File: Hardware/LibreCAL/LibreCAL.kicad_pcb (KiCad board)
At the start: 4 copper layers, 55 x 73.5 mm, 132 parts, among them J1 901-10510-2, J2 901-10510-2, J3 901-10510-2, J4 901-10510-2, J5 USB_C_Receptacle_USB2.0, J6 TC2030-ARM, Q1 IRLML2060, SW1 TL3301NF160QG, SW2 TL3301CF160QG, SW3 TL3301CF160QG, U1 PE426462, U2 PE426462, U3 PE426462, U4 PE426462, U5 W25Q16JVSNIQ, U6 IP4234CZ6, U7 RP2040, U8 W25Q16JVSNIQ, U9 MIC5528-3.3YMT-TR, Y1 ECS-120-8-36-CKM-TR3

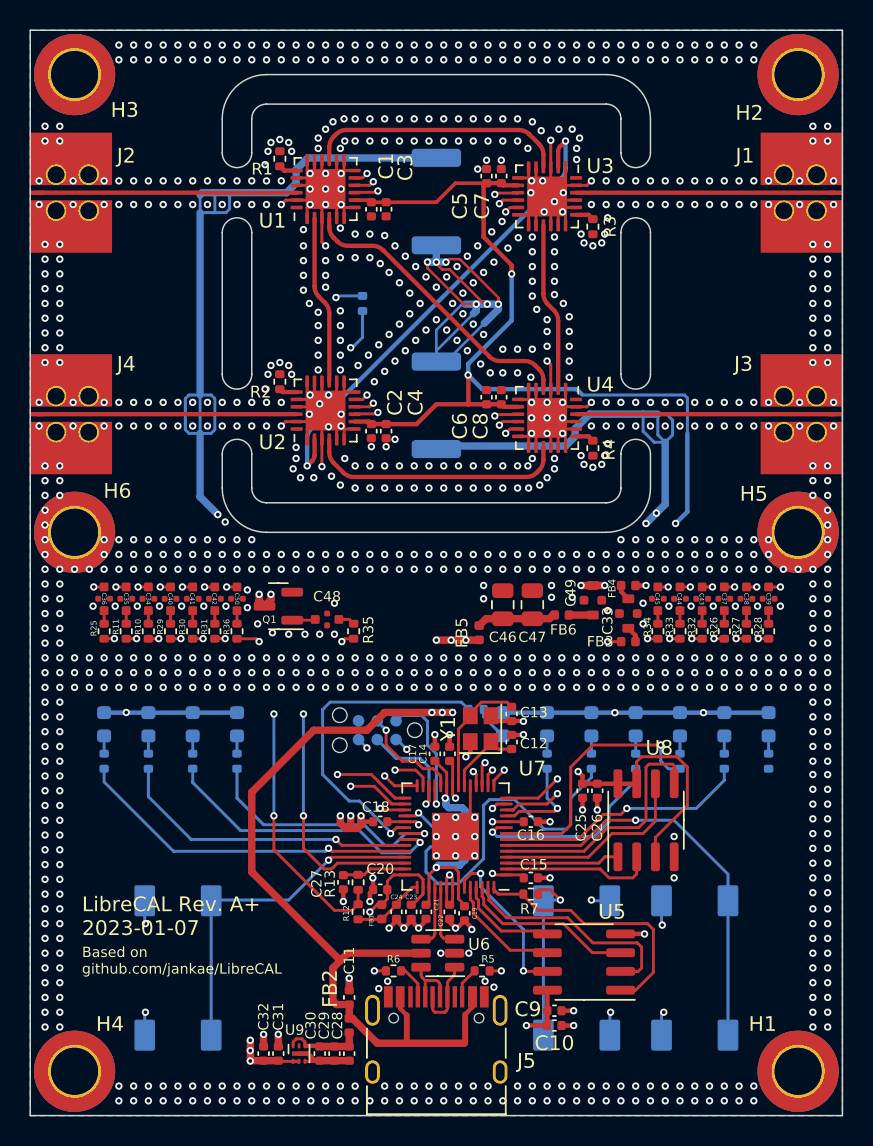
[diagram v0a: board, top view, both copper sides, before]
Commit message: update to larger flash for calibration coefficients
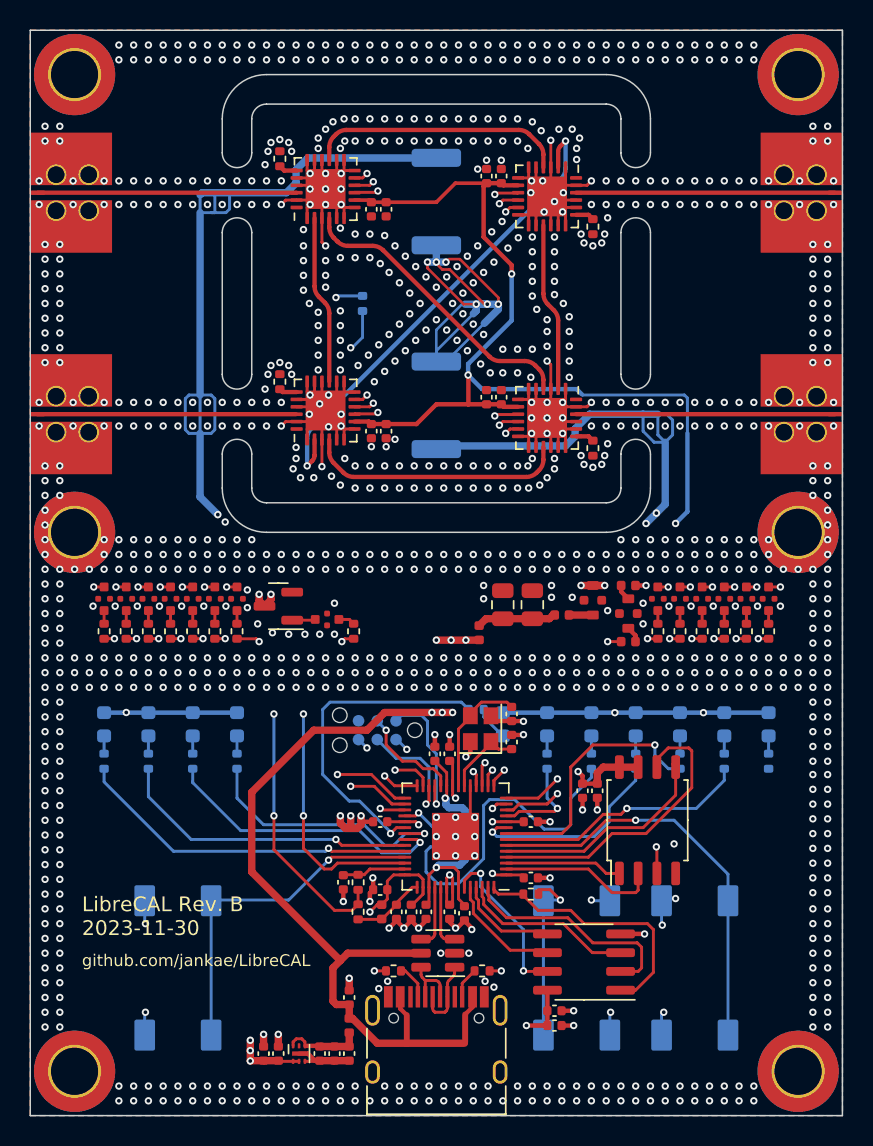
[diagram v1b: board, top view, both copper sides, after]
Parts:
- U8: value W25Q16JVSNIQ -> W25Q128JVSIQ; footprint Package_SO:SOIC-8_3.9x4.9mm_P1.27mm -> Package_SO:SOIC-8_5.23x5.23mm_P1.27mm
- moved U8 0.10 mm to (141.8, 119.5)
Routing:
- net +3V3: track 80.5 -> 71.0 mm, vias 16 -> 17
- net Net-(U7-GPIO2): track 13.6 -> 20.3 mm
- net Net-(U7-GPIO3): track 17.2 -> 15.1 mm
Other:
- board text added: "github.com/jankae/LibreCAL"
- board text removed: "Based on github.com/jankae/LibreCAL"
